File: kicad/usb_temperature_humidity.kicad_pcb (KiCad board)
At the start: 2 copper layers, 72 x 47.5 mm, 22 parts, among them J1 Conn_01x01, J10 Conn_01x01, J11 Conn_01x01, J12 Conn_01x01, J13 Conn_01x01, J14 Conn_01x01, J2 Conn_01x01, J3 Conn_01x01, J4 Conn_01x01, J5 Conn_01x01, J6 Conn_01x01, J7 Conn_01x01, J8 Conn_01x01, J9 Conn_01x01, SW1 SW_SPDT, SW2 SW_SPDT, U1 SeeeduinoXIAO, U2 SHT-31

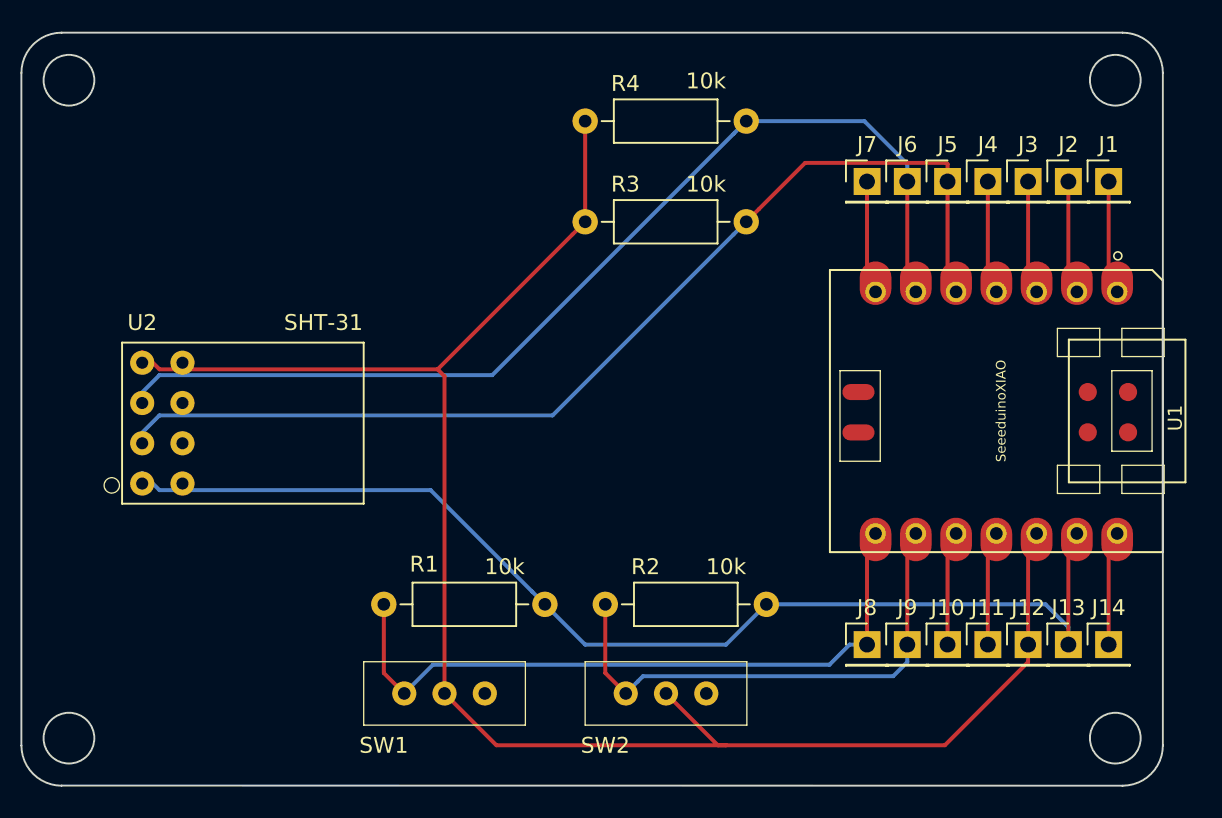
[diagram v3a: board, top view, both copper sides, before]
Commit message: REALGLOBEのロゴを入れた
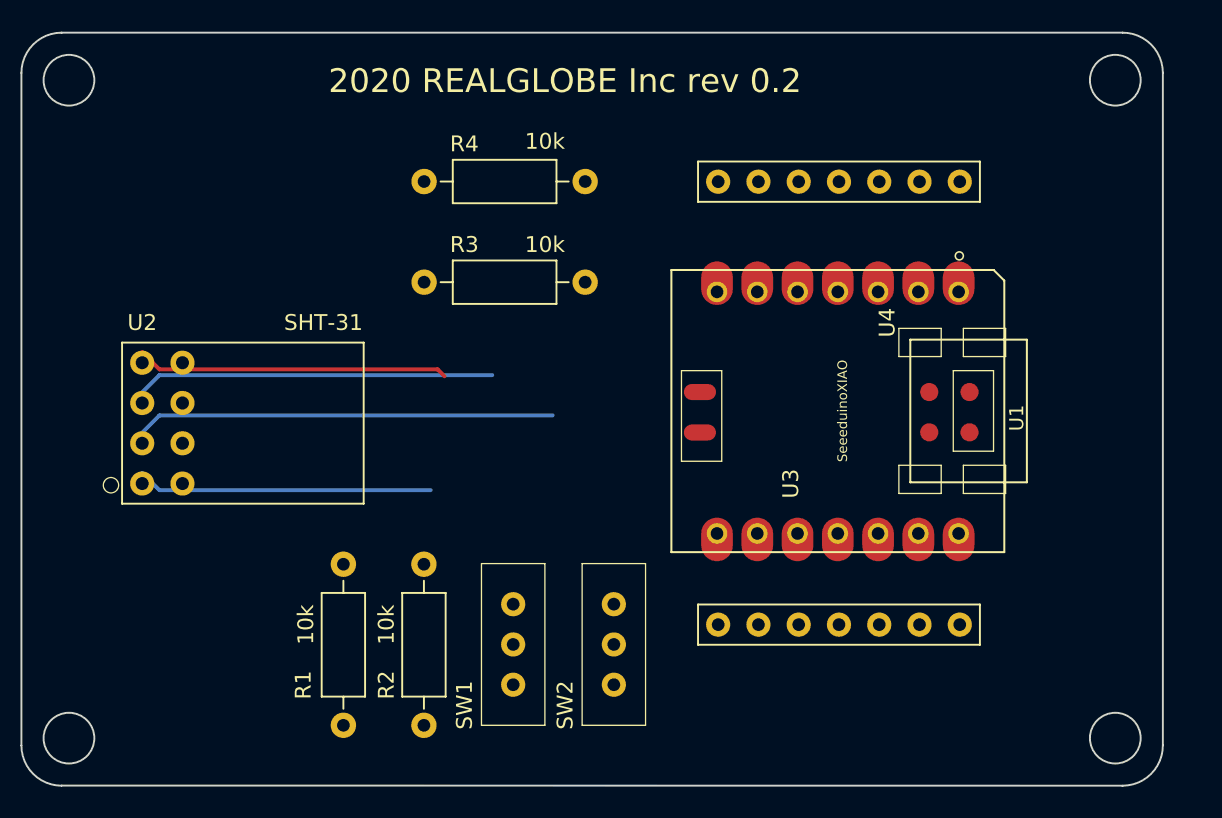
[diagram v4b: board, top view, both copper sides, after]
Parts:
- removed J1, J10, J11, J12, J13, J14, J2, J3, J4, J5, J6, J7, J8, J9: Conn_01x01, Connector_PinHeader_2.54mm:PinHeader_1x01_P2.54mm_Vertical
- added U3: PinHeader_XIAO, kicad_mylib:PinHeader_XIAO, F.Cu at (42.7, -11.4)
- added U4: PinHeader_XIAO, kicad_mylib:PinHeader_XIAO, F.Cu at (60.5, -36.8)
- moved R2 13.8 mm to (25.4, -3.81), turned to 90 degrees
- moved SW1 11.4 mm to (33.0, -3.81), turned to 90 degrees
- moved R3 10.9 mm to (25.4, -31.8)
- moved R4 10.9 mm to (25.4, -38.1)
- moved U1 10.0 mm to (41.0, -32.5)
- moved R1 8.04 mm to (20.3, -3.81), turned to 90 degrees
- moved SW2 3.81 mm to (39.4, -3.81), turned to 90 degrees
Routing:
- net +3V3: track 112.7 -> 19.7 mm
- net GND: track 72.5 -> 18.6 mm
- net Net-(R1-Pad1): track 43.5 -> 0.00 mm
- net Net-(R4-Pad2): track 64.2 -> 22.5 mm
- net Net-(R3-Pad2): track 65.6 -> 26.3 mm
- net Net-(R2-Pad1): track 32.7 -> 0.00 mm
- net Net-(U1-Pad14): track 6.86 -> 0.00 mm
- net Net-(U1-Pad11): track 6.86 -> 0.00 mm
- net Net-(U1-Pad10): track 6.86 -> 0.00 mm
- net Net-(U1-Pad7): track 6.64 -> 0.00 mm
- net Net-(U1-Pad4): track 6.64 -> 0.00 mm
- net Net-(U1-Pad3): track 6.64 -> 0.00 mm
- net Net-(U1-Pad2): track 6.64 -> 0.00 mm
- net Net-(U1-Pad1): track 6.64 -> 0.00 mm
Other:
- board text added: "2020 REALGLOBE Inc rev 0.2"
- board text removed: "○"

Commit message: DRC OK
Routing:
- net +3V3: track 19.7 -> 83.2 mm
- net Net-(R4-Pad2): track 22.5 -> 54.3 mm
- net Net-(R1-Pad1): track 0.00 -> 31.7 mm
- net Net-(R2-Pad1): track 0.00 -> 29.1 mm
- net Net-(R3-Pad2): track 26.3 -> 55.4 mm
- net Net-(U1-Pad7): track 0.00 -> 6.43 mm
- net Net-(U1-Pad4): track 0.00 -> 6.43 mm
- net Net-(U1-Pad3): track 0.00 -> 6.43 mm
- net Net-(U1-Pad2): track 0.00 -> 6.43 mm
- net Net-(U1-Pad1): track 0.00 -> 6.43 mm
- net Net-(U1-Pad11): track 0.00 -> 5.40 mm
- net Net-(U1-Pad10): track 0.00 -> 5.40 mm
- net Net-(U1-Pad14): track 0.00 -> 5.40 mm
- net GND: track 18.6 -> 22.7 mm
- added copper zone on B.Cu, net GND
- added copper zone on F.Cu, net GND
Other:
- outline, holes or cut-outs redrawn
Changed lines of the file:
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@@
   (general
     (thickness 1.6)
-    (drawings 18)
-    (tracks 9)
+    (drawings 22)
+    (tracks 72)
     (zones 0)
     (modules 10)
@@
     )
   )
+  (gr_line (start 62.23 -33) (end 72 -33) (layer Edge.Cuts) (width 0.12))
+  (gr_line (start 62.23 -14) (end 72 -14) (layer Edge.Cuts) (width 0.12))
+  (gr_line (start 62.23 -33) (end 62.23 -14) (layer Edge.Cuts) (width 0.12))
+  (gr_line (start 72 -44.96) (end 72 -33) (layer Edge.Cuts) (width 0.12))
   (gr_text "2020 REALGLOBE Inc rev 0.2" (at 34.29 -44.45) (layer F.SilkS)
     (effects (font (size 1.5 1.5) (thickness 0.3)))
@@
   (gr_circle (center 3 -44.5) (end 4.6 -44.5) (layer Edge.Cuts) (width 0.12))
   (gr_circle (center 3 -3) (end 4.6 -3) (layer Edge.Cuts) (width 0.12))
-  (gr_arc (start 2.54 -2.54) (end 2.54 0) (angle 90) (layer Edge.Cuts) (width 0.12))
+  (gr_arc (start 2.54 -2.54) (end 2.54 -0.01) (angle 90) (layer Edge.Cuts) (width 0.12))
   (gr_line (start 2.54 -0.01) (end 69.46 0) (layer Edge.Cuts) (width 0.12))
-  (gr_line (start 72 -44.96) (end 72 -2.54) (layer Edge.Cuts) (width 0.12))
-  (gr_line (start 0 -44.96) (end 0 -2.54) (layer Edge.Cuts) (width 0.12))
-  (segment (start 8.707001 -18.642999) (end 25.817001 -18.642999) (width 0.25) (layer B.Cu) (net 1))
-  (segment (start 7.62 -19.73) (end 8.707001 -18.642999) (width 0.25) (layer B.Cu) (net 1))
-  (segment (start 8.707001 -23.357001) (end 33.507001 -23.357001) (width 0.25) (layer B.Cu) (net 15))
-  (segment (start 7.62 -22.27) (end 8.707001 -23.357001) (width 0.25) (layer B.Cu) (net 15))
-  (segment (start 8.707001 -26.262999) (end 26.252999 -26.262999) (width 0.25) (layer F.Cu) (net 2))
-  (segment (start 7.62 -27.35) (end 8.707001 -26.262999) (width 0.25) (layer F.Cu) (net 2))
-  (segment (start 26.69 -25.825998) (end 26.252999 -26.262999) (width 0.25) (layer F.Cu) (net 2))
-  (segment (start 8.707001 -25.897001) (end 29.697001 -25.897001) (width 0.25) (layer B.Cu) (net 16))
-  (segment (start 7.62 -24.81) (end 8.707001 -25.897001) (width 0.25) (layer B.Cu) (net 16))
+  (gr_line (start 72 -14) (end 72 -2.54) (layer Edge.Cuts) (width 0.12))
+  (gr_line (start 0 -44.96) (end 0.01 -2.54) (layer Edge.Cuts) (width 0.12))
+  (segment (start 56.65 -15.46014) (end 56.57782 -15.53232) (width 0.25) (layer F.Cu) (net 1))
+  (segment (start 56.65 -10.16) (end 56.65 -15.46014) (width 0.25) (layer F.Cu) (net 1))
+  (segment (start 10.16 -21.6) (end 10.16 -19.06) (width 0.25) (layer F.Cu) (net 1))
+  (segment (start 7.62 -19.06) (end 10.16 -19.06) (width 0.25) (layer F.Cu) (net 1))
+  (segment (start 15.22 -19.06) (end 20.31 -13.97) (width 0.25) (layer F.Cu) (net 1))
+  (segment (start 10.16 -19.06) (end 15.22 -19.06) (width 0.25) (layer F.Cu) (net 1))
+  (segment (start 54.11 -15.46014) (end 54.03782 -15.53232) (width 0.25) (layer F.Cu) (net 2))
+  (segment (start 54.11 -10.16) (end 54.11 -15.46014) (width 0.25) (layer F.Cu) (net 2))
+  (segment (start 38.66 -7.62) (end 37.37 -8.91) (width 0.25) (layer F.Cu) (net 2))
+  (segment (start 54.11 -9.08237) (end 52.64763 -7.62) (width 0.25) (layer F.Cu) (net 2))
+  (segment (start 52.64763 -7.62) (end 38.66 -7.62) (width 0.25) (layer F.Cu) (net 2))
+  (segment (start 54.11 -10.16) (end 54.11 -9.08237) (width 0.25) (layer F.Cu) (net 2))
+  (segment (start 32.31 -7.62) (end 31.02 -8.91) (width 0.25) (layer F.Cu) (net 2))
+  (segment (start 36.08 -7.62) (end 32.31 -7.62) (width 0.25) (layer F.Cu) (net 2))
+  (segment (start 37.37 -8.91) (end 36.08 -7.62) (width 0.25) (layer F.Cu) (net 2))
+  (segment (start 31.02 -8.91) (end 27.94 -11.99) (width 0.25) (layer F.Cu) (net 2))
+  (segment (start 27.94 -29.22) (end 25.4 -31.76) (width 0.25) (layer F.Cu) (net 2))
+  (segment (start 27.94 -11.99) (end 27.94 -29.22) (width 0.25) (layer F.Cu) (net 2))
+  (segment (start 25.4 -38.11) (end 25.4 -31.76) (width 0.25) (layer F.Cu) (net 2))
+  (segment (start 12.7 -31.76) (end 7.62 -26.68) (width 0.25) (layer F.Cu) (net 2))
+  (segment (start 25.4 -31.76) (end 12.7 -31.76) (width 0.25) (layer F.Cu) (net 2))
+  (segment (start 43.95 -15.46014) (end 43.87782 -15.53232) (width 0.25) (layer F.Cu) (net 13))
+  (segment (start 43.95 -10.16) (end 43.95 -15.46014) (width 0.25) (layer F.Cu) (net 13))
+  (segment (start 31.781999 -7.131999) (end 31.02 -6.37) (width 0.25) (layer B.Cu) (net 13))
+  (segment (start 32.472999 -7.822999) (end 31.781999 -7.131999) (width 0.25) (layer B.Cu) (net 13))
+  (segment (start 41.612999 -7.822999) (end 32.472999 -7.822999) (width 0.25) (layer B.Cu) (net 13))
+  (segment (start 43.95 -10.16) (end 41.612999 -7.822999) (width 0.25) (layer B.Cu) (net 13))
+  (segment (start 22.87 -6.37) (end 20.31 -3.81) (width 0.25) (layer B.Cu) (net 13))
+  (segment (start 31.02 -6.37) (end 22.87 -6.37) (width 0.25) (layer B.Cu) (net 13))
+  (segment (start 46.49 -15.46014) (end 46.41782 -15.53232) (width 0.25) (layer F.Cu) (net 14))
+  (segment (start 46.49 -10.16) (end 46.49 -15.46014) (width 0.25) (layer F.Cu) (net 14))
+  (segment (start 42.7 -6.37) (end 37.37 -6.37) (width 0.25) (layer B.Cu) (net 14))
+  (segment (start 46.49 -10.16) (end 42.7 -6.37) (width 0.25) (layer B.Cu) (net 14))
+  (segment (start 34.81 -3.81) (end 25.39 -3.81) (width 0.25) (layer B.Cu) (net 14))
+  (segment (start 37.37 -6.37) (end 34.81 -3.81) (width 0.25) (layer B.Cu) (net 14))
+  (segment (start 49.03 -31.76906) (end 48.95782 -31.69688) (width 0.25) (layer F.Cu) (net 15))
+  (segment (start 49.03 -38.1) (end 49.03 -31.76906) (width 0.25) (layer F.Cu) (net 15))
+  (segment (start 34.760001 -30.960001) (end 35.56 -31.76) (width 0.25) (layer B.Cu) (net 15))
+  (segment (start 24.12 -20.32) (end 34.760001 -30.960001) (width 0.25) (layer B.Cu) (net 15))
+  (segment (start 8.9 -20.32) (end 24.12 -20.32) (width 0.25) (layer B.Cu) (net 15))
+  (segment (start 7.62 -21.6) (end 8.9 -20.32) (width 0.25) (layer B.Cu) (net 15))
+  (segment (start 45.818 -34.29) (end 48.308001 -31.799999) (width 0.25) (layer B.Cu) (net 15))
+  (segment (start 38.09 -34.29) (end 45.818 -34.29) (width 0.25) (layer B.Cu) (net 15))
+  (segment (start 48.308001 -31.799999) (end 48.958 -31.15) (width 0.25) (layer B.Cu) (net 15))
+  (segment (start 35.56 -31.76) (end 38.09 -34.29) (width 0.25) (layer B.Cu) (net 15))
+  (segment (start 46.49 -31.76906) (end 46.41782 -31.69688) (width 0.25) (layer F.Cu) (net 16))
+  (segment (start 46.49 -38.1) (end 46.49 -31.76906) (width 0.25) (layer F.Cu) (net 16))
+  (segment (start 36.82 -39.37) (end 36.83 -39.37) (width 0.25) (layer B.Cu) (net 16))
+  (segment (start 35.56 -38.11) (end 36.82 -39.37) (width 0.25) (layer B.Cu) (net 16))
+  (segment (start 36.83 -39.37) (end 38.1 -40.64) (width 0.25) (layer B.Cu) (net 16))
+  (segment (start 43.95 -40.64) (end 46.49 -38.1) (width 0.25) (layer B.Cu) (net 16))
+  (segment (start 38.1 -40.64) (end 43.95 -40.64) (width 0.25) (layer B.Cu) (net 16))
+  (segment (start 34.760001 -37.310001) (end 35.56 -38.11) (width 0.25) (layer B.Cu) (net 16))
+  (segment (start 20.31 -22.86) (end 34.760001 -37.310001) (width 0.25) (layer B.Cu) (net 16))
+  (segment (start 8.9 -22.86) (end 20.31 -22.86) (width 0.25) (layer B.Cu) (net 16))
+  (segment (start 7.62 -24.14) (end 8.9 -22.86) (width 0.25) (layer B.Cu) (net 16))
+  (segment (start 49.03 -15.46014) (end 48.95782 -15.53232) (width 0.25) (layer F.Cu) (net 17))
+  (segment (start 49.03 -10.16) (end 49.03 -15.46014) (width 0.25) (layer F.Cu) (net 17))
+  (segment (start 51.57 -15.46014) (end 51.49782 -15.53232) (width 0.25) (layer F.Cu) (net 18))
+  (segment (start 51.57 -10.16) (end 51.57 -15.46014) (width 0.25) (layer F.Cu) (net 18))
+  (segment (start 59.19 -15.46014) (end 59.11782 -15.53232) (width 0.25) (layer F.Cu) (net 19))
+  (segment (start 59.19 -10.16) (end 59.19 -15.46014) (width 0.25) (layer F.Cu) (net 19))
+  (segment (start 43.95 -31.76906) (end 43.87782 -31.69688) (width 0.25) (layer F.Cu) (net 20))
+  (segment (start 43.95 -38.1) (end 43.95 -31.76906) (width 0.25) (layer F.Cu) (net 20))
+  (segment (start 51.57 -31.76906) (end 51.49782 -31.69688) (width 0.25) (layer F.Cu) (net 21))
+  (segment (start 51.57 -38.1) (end 51.57 -31.76906) (width 0.25) (layer F.Cu) (net 21))
+  (segment (start 54.11 -31.76906) (end 54.03782 -31.69688) (width 0.25) (layer F.Cu) (net 22))
+  (segment (start 54.11 -38.1) (end 54.11 -31.76906) (width 0.25) (layer F.Cu) (net 22))
+  (segment (start 56.65 -31.76906) (end 56.57782 -31.69688) (width 0.25) (layer F.Cu) (net 23))
+  (segment (start 56.65 -38.1) (end 56.65 -31.76906) (width 0.25) (layer F.Cu) (net 23))
+  (segment (start 59.19 -31.76906) (end 59.11782 -31.69688) (width 0.25) (layer F.Cu) (net 24))
+  (segment (start 59.19 -38.1) (end 59.19 -31.76906) (width 0.25) (layer F.Cu) (net 24))
   (zone (net 0) (net_name "") (layers F&B.Cu) (hatch edge 0.508)
     (connect_pads (clearance 0.508))
@@
       )
     )
+  )
+  (zone (net 1) (net_name GND) (layer F.Cu) (hatch edge 0.508)
+    (connect_pads (clearance 0.508))
+    (min_thickness 0.254)
+    (fill yes (arc_segments 32) (thermal_gap 0.508) (thermal_bridge_width 0.508))
+    (polygon
+      (pts
+        (xy 73.66 -49.53) (xy -2.54 -49.53) (xy -2.54 2.54) (xy 73.66 2.54)
+      )
+    )
+  )
+  (zone (net 1) (net_name GND) (layer B.Cu) (hatch edge 0.508)
+    (connect_pads (clearance 0.508))
+    (min_thickness 0.254)
+    (fill yes (arc_segments 32) (thermal_gap 0.508) (thermal_bridge_width 0.508))
+    (polygon
+      (pts
+        (xy 76.2 -52.07) (xy -3.81 -52.07) (xy -3.81 3.81) (xy 76.2 3.81)
+      )
+    )

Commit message: DRD OK
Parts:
- added JP1: SolderJumper_2_Open, Jumper:SolderJumper-2_P1.3mm_Open_TrianglePad1.0x1.5mm, F.Cu at (36.3, -27.9)
- added JP2: SolderJumper_2_Open, Jumper:SolderJumper-2_P1.3mm_Open_TrianglePad1.0x1.5mm, F.Cu at (31.8, -27.9)
- added R5: R, Resistor_THT:R_Axial_DIN0207_L6.3mm_D2.5mm_P10.16mm_Horizontal, F.Cu at (29.3, -22.9)
- added R6: R, Resistor_THT:R_Axial_DIN0207_L6.3mm_D2.5mm_P10.16mm_Horizontal, F.Cu at (29.3, -17.3)
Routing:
- net Net-(JP2-Pad1): track 6.43 -> 40.9 mm
- net Net-(JP1-Pad2): track 0.00 -> 29.3 mm
- net Net-(JP2-Pad2): track 0.00 -> 25.4 mm
- net Net-(JP1-Pad1): track 6.43 -> 29.1 mm
- net Net-(R3-Pad2): track 55.4 -> 62.7 mm
- net Net-(R4-Pad2): track 54.3 -> 59.5 mm
